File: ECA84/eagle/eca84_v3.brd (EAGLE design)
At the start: 222.9 x 127 mm, 186 parts

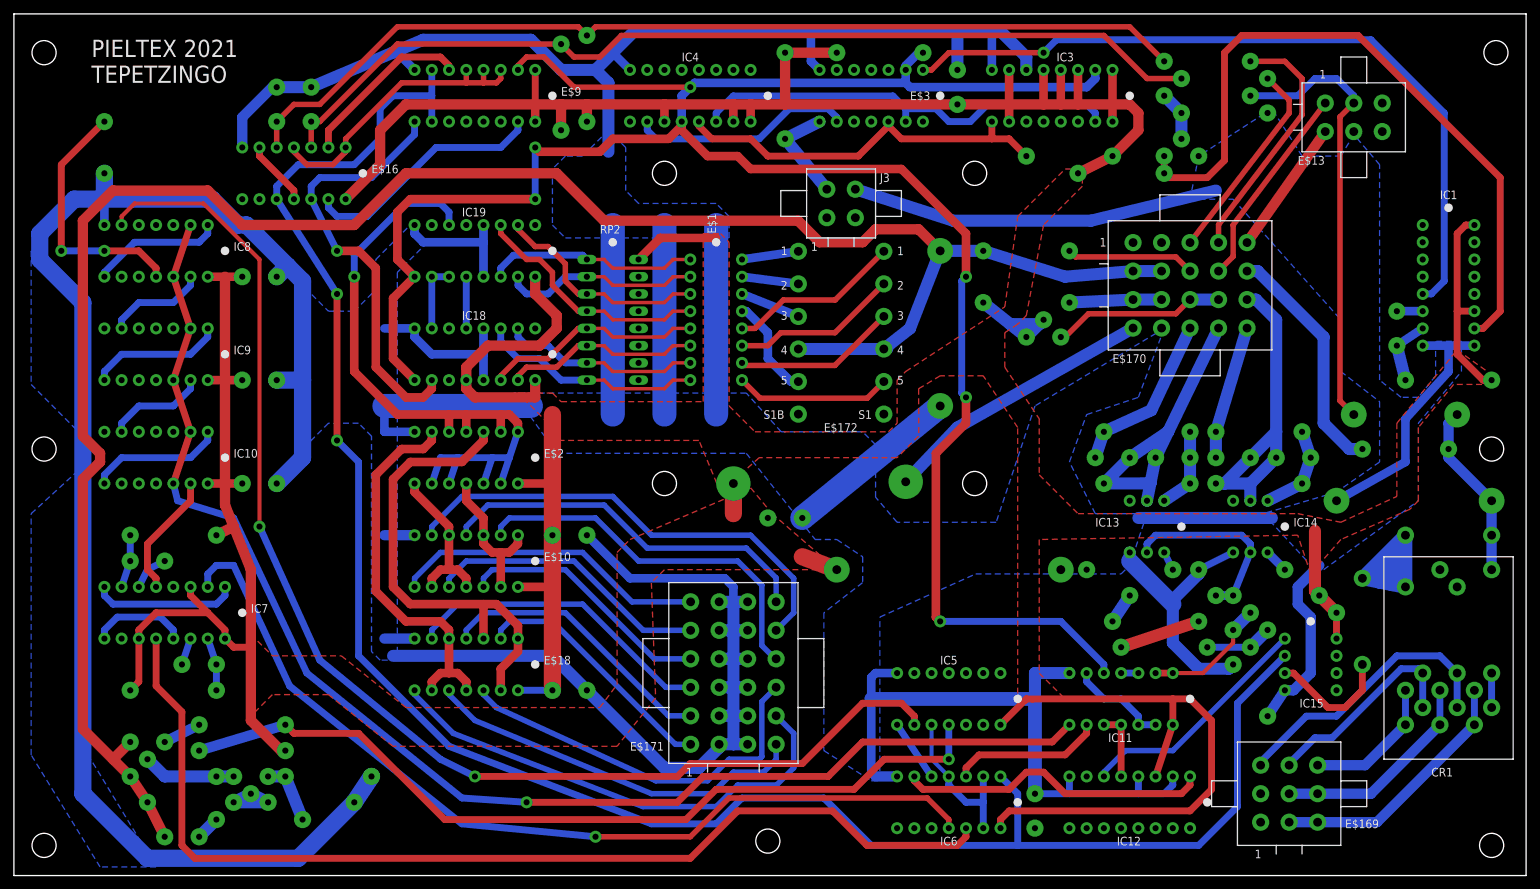
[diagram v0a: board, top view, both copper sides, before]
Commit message: ajustar orificios y exportar archivos CAM
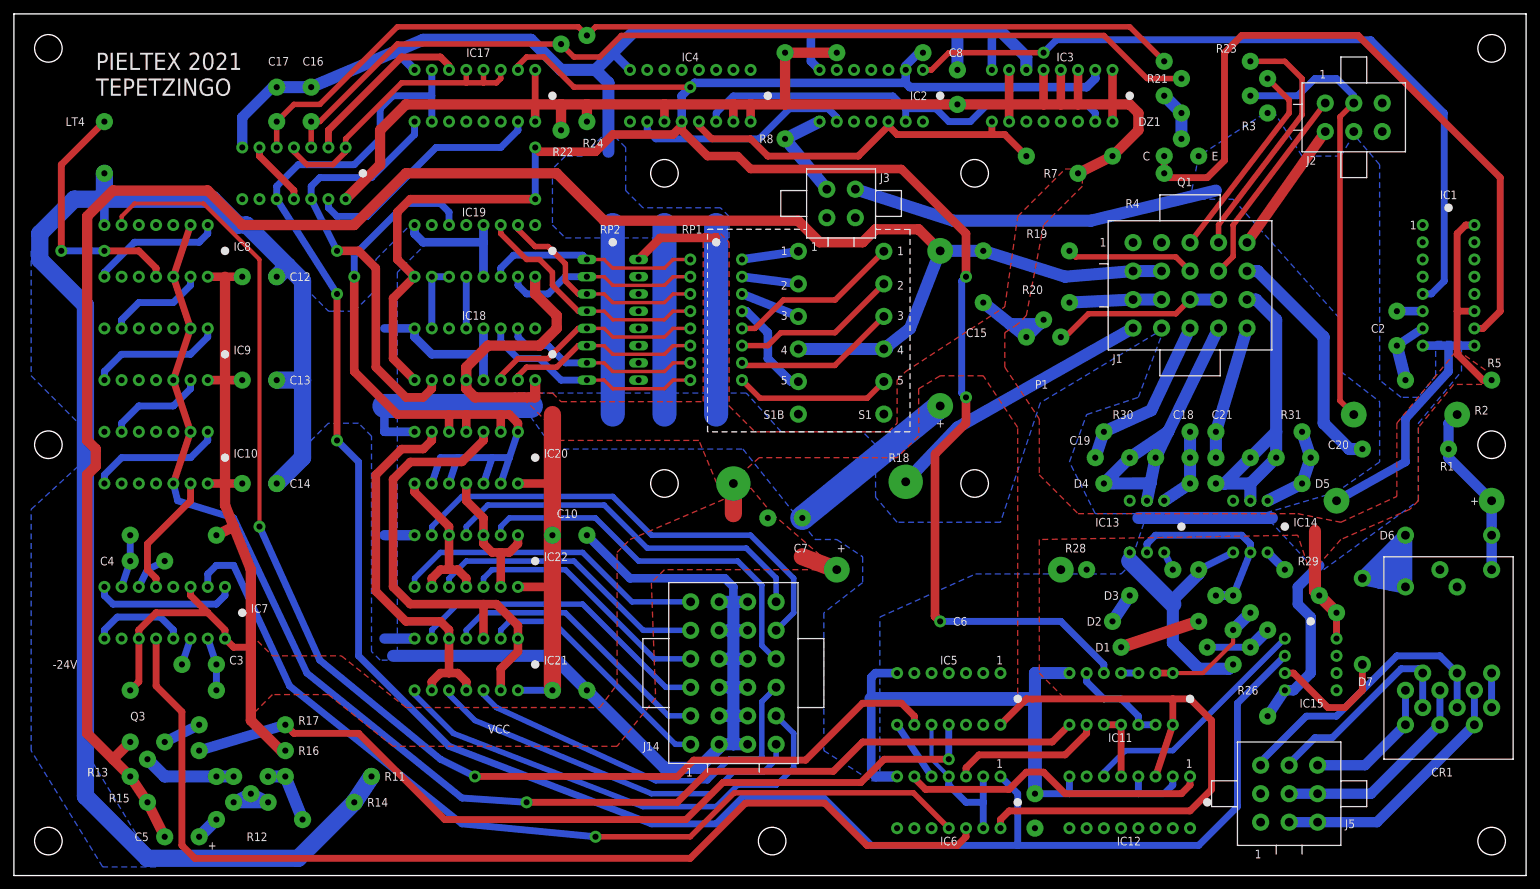
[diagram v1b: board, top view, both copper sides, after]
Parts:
- renumbered E$1 to RP1, E$10 to IC22, E$13 to J2, E$169 to J5, E$170 to J1, E$171 to J14, E$18 to IC21, E$2 to IC20, E$3 to IC2, E$9 to IC17
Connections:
- removed net S$45: IC11.P$14, IC12.P$3, IC5.P$14, IC6.P$14
- net VCC: now also IC11.P$14, IC12.P$3, IC5.P$14, IC6.P$14
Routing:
- net VCC: track 499.6 -> 589.9 mm
- net S$45: track 90.2 -> 0.00 mm
- net S$114: track 304.2 -> 302.6 mm
- net S$10: track 155.2 -> 156.2 mm
- net S$23: track 57.6 -> 57.0 mm
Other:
- board text added: "+"
- board text added: "-24V"
- board text added: "1"
- board text added: "C"
- board text added: "C10"
- board text added: "C12"
- board text added: "C13"
- board text added: "C14"
- board text added: "C15"
- board text added: "C16"
- board text added: "C17"
- board text added: "C18"
- board text added: "C19"
- board text added: "C2"
- board text added: "C20"
- board text added: "C21"
- board text added: "C3"
- board text added: "C4"
- board text added: "C5"
- board text added: "C6"
- board text added: "C7"
- board text added: "C8"
- board text added: "D1"
- board text added: "D2"
- board text added: "D3"
- board text added: "D4"
- board text added: "D5"
- board text added: "D6"
- board text added: "D7"
- board text added: "DZ1"
- board text added: "E"
- board text added: "LT4"
- board text added: "P1"
- board text added: "Q1"
- board text added: "Q3"
- board text added: "R1"
- board text added: "R11"
- board text added: "R12"
- board text added: "R13"
- board text added: "R14"
- board text added: "R15"
- board text added: "R16"
- board text added: "R17"
- board text added: "R18"
- board text added: "R19"
- board text added: "R2"
- board text added: "R20"
- board text added: "R21"
- board text added: "R22"
- board text added: "R23"
- board text added: "R24"
- board text added: "R26"
- board text added: "R28"
- board text added: "R29"
- board text added: "R3"
- board text added: "R30"
- board text added: "R31"
- board text added: "R4"
- board text added: "R5"
- board text added: "R7"
- board text added: "R8"
- board text added: "VCC"

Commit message: corrección pistas faltantes
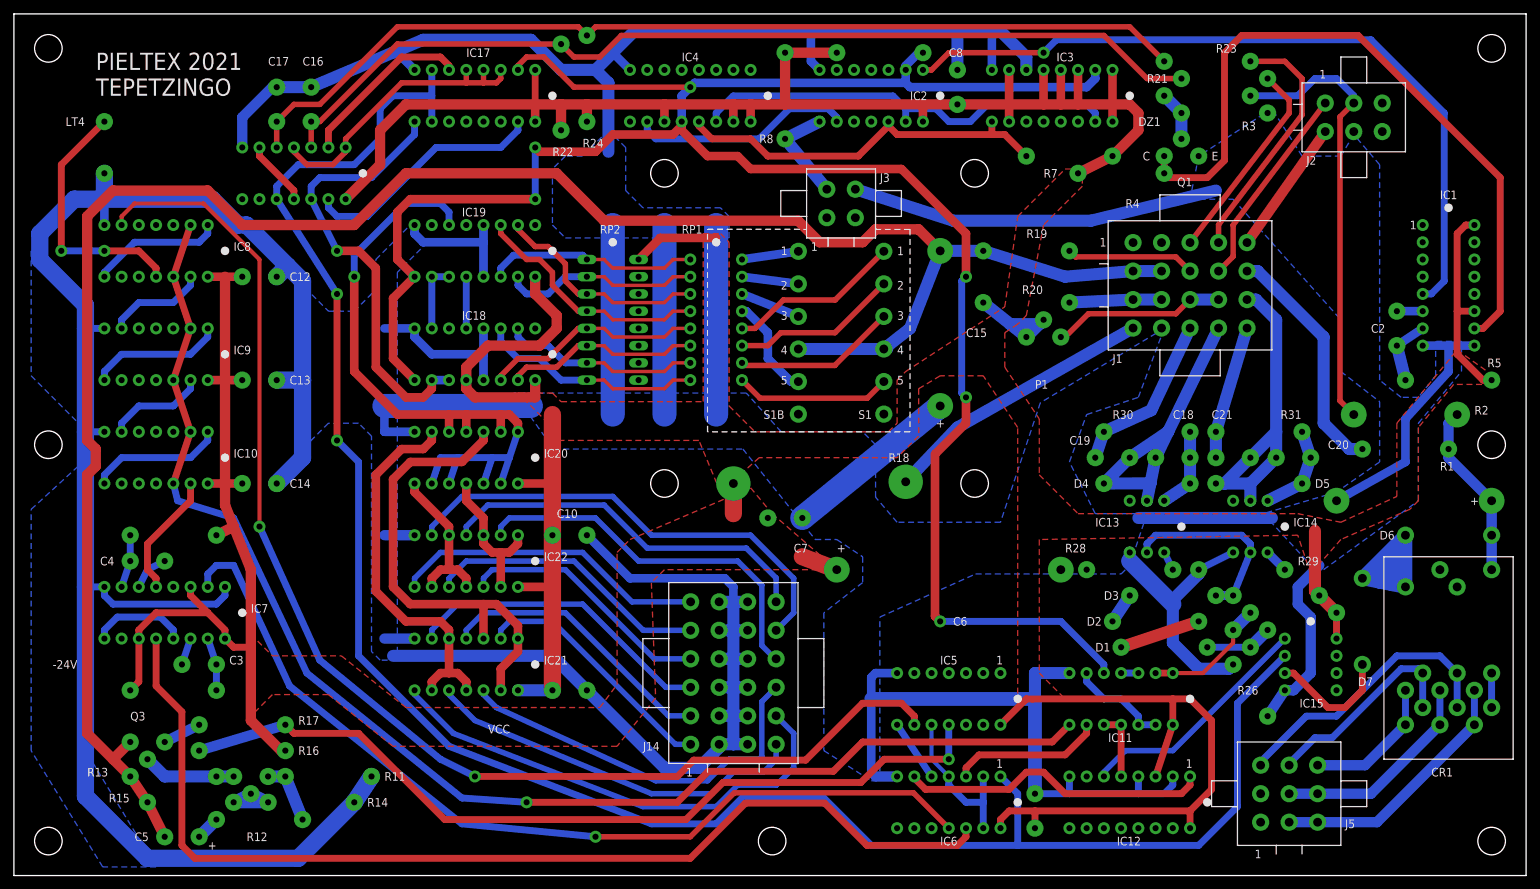
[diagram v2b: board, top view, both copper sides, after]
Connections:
- removed net S$57: IC7.P$1, IC7.P$8
- net GND: now also IC10.P$7, IC7.P$1, IC7.P$8, IC9.P$7
- net S$24: now also IC18.P$11
- net VCC: now also E$148.P$1, IC12.P$16, IC2.P$14
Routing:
- net GND: track 995.7 -> 1025.5 mm
- net S$57: track 21.4 -> 0.00 mm
- net VCC: track 589.9 -> 597.5 mm
- net S$24: track 64.0 -> 66.5 mm
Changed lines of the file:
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@@
 <wire x1="151.765" y1="118.745" x2="151.765" y2="113.665" width="1.27" layer="1"/>
 <contactref element="E$83" pad="P$1"/>
-<wire x1="113.665" y1="113.665" x2="139.065" y2="113.665" width="1.524" layer="1"/>
+<wire x1="113.665" y1="113.665" x2="133.985" y2="113.665" width="1.524" layer="1"/>
+<wire x1="133.985" y1="113.665" x2="139.065" y2="113.665" width="1.524" layer="1"/>
 <wire x1="139.065" y1="113.665" x2="146.685" y2="113.665" width="1.524" layer="1"/>
 <wire x1="146.685" y1="113.665" x2="151.765" y2="113.665" width="1.524" layer="1"/>
@@
 <wire x1="161.925" y1="106.045" x2="156.845" y2="103.505" width="1.524" layer="1"/>
 <contactref element="IC21" pad="P$14"/>
-<wire x1="74.295" y1="27.305" x2="79.375" y2="27.305" width="1.016" layer="16"/>
+<wire x1="74.295" y1="27.305" x2="79.375" y2="27.305" width="1.778" layer="16"/>
 <contactref element="E$14" pad="P$1"/>
 <wire x1="121.285" y1="45.085" x2="116.205" y2="46.99" width="2.54" layer="1"/>
@@
 <wire x1="145.415" y1="6.985" x2="145.415" y2="8.255" width="1.016" layer="1"/>
 <wire x1="145.415" y1="8.255" x2="146.685" y2="9.525" width="1.016" layer="1"/>
-<wire x1="146.685" y1="9.525" x2="173.355" y2="9.525" width="1.016" layer="1"/>
+<wire x1="146.685" y1="9.525" x2="150.495" y2="9.525" width="1.016" layer="1"/>
+<wire x1="150.495" y1="9.525" x2="173.355" y2="9.525" width="1.016" layer="1"/>
 <wire x1="173.355" y1="9.525" x2="176.53" y2="12.7" width="1.016" layer="1"/>
 <wire x1="176.53" y1="12.7" x2="176.53" y2="22.86" width="1.016" layer="1"/>
@@
 <contactref element="IC12" pad="P$3"/>
 <wire x1="168.275" y1="14.605" x2="170.815" y2="22.225" width="1.016" layer="1"/>
+<contactref element="E$148" pad="P$1"/>
+<contactref element="IC12" pad="P$16"/>
+<wire x1="150.495" y1="6.985" x2="150.495" y2="9.525" width="1.016" layer="1"/>
+<wire x1="173.355" y1="6.985" x2="173.355" y2="9.525" width="1.016" layer="1"/>
+<contactref element="IC2" pad="P$14"/>
+<wire x1="133.985" y1="111.125" x2="133.985" y2="113.665" width="1.27" layer="1"/>
 </signal>
 <signal name="S$10">
@@
 <wire x1="64.135" y1="97.79" x2="64.135" y2="95.885" width="1.016" layer="16"/>
 </signal>
-<signal name="S$24">
-<contactref element="E$58" pad="P$1"/>
-<wire x1="47.625" y1="92.075" x2="50.8" y2="92.075" width="1.27" layer="1"/>
-<wire x1="50.8" y1="92.075" x2="53.34" y2="89.535" width="1.27" layer="1"/>
-<wire x1="53.34" y1="89.535" x2="53.34" y2="74.93" width="1.27" layer="1"/>
-<wire x1="53.34" y1="74.93" x2="57.785" y2="70.485" width="1.27" layer="1"/>
-<wire x1="57.785" y1="70.485" x2="60.325" y2="70.485" width="1.27" layer="1"/>
-<contactref element="IC18" pad="P$10"/>
-<wire x1="60.325" y1="70.485" x2="61.595" y2="71.755" width="1.27" layer="1"/>
-<wire x1="61.595" y1="71.755" x2="61.595" y2="73.025" width="1.27" layer="1"/>
-<contactref element="E$16" pad="P$12"/>
-<contactref element="IC17" pad="P$9"/>
-<wire x1="43.815" y1="99.695" x2="43.815" y2="101.6" width="1.016" layer="16"/>
-<wire x1="43.815" y1="101.6" x2="45.085" y2="102.87" width="1.016" layer="16"/>
-<wire x1="45.085" y1="102.87" x2="52.705" y2="102.87" width="1.016" layer="16"/>
-<wire x1="52.705" y1="102.87" x2="59.055" y2="109.22" width="1.016" layer="16"/>
-<wire x1="59.055" y1="109.22" x2="59.055" y2="111.125" width="1.016" layer="16"/>
-<wire x1="47.625" y1="92.075" x2="43.815" y2="99.695" width="1.016" layer="16"/>
-</signal>
 <signal name="S$26">
 <contactref element="IC19" pad="P$2"/>
@@
 <wire x1="23.495" y1="36.195" x2="23.495" y2="34.925" width="1.016" layer="16"/>
 </signal>
-<signal name="S$57">
-<contactref element="IC7" pad="P$1"/>
-<contactref element="IC7" pad="P$8"/>
-<wire x1="13.335" y1="42.545" x2="13.335" y2="41.275" width="1.016" layer="16"/>
-<wire x1="13.335" y1="41.275" x2="14.605" y2="40.005" width="1.016" layer="16"/>
-<wire x1="14.605" y1="40.005" x2="29.845" y2="40.005" width="1.016" layer="16"/>
-<wire x1="29.845" y1="40.005" x2="31.115" y2="41.275" width="1.016" layer="16"/>
-<wire x1="31.115" y1="41.275" x2="31.115" y2="42.545" width="1.016" layer="16"/>
-</signal>
 <signal name="S$58">
 <contactref element="E$30" pad="P$1"/>
@@
 <wire x1="8.89" y1="99.695" x2="3.81" y2="94.615" width="2.54" layer="16"/>
 <wire x1="3.81" y1="90.805" x2="10.541" y2="84.074" width="2.54" layer="16"/>
-<wire x1="10.541" y1="84.074" x2="10.541" y2="11.684" width="2.54" layer="16"/>
+<wire x1="10.541" y1="84.074" x2="10.541" y2="80.645" width="2.54" layer="16"/>
+<wire x1="10.541" y1="80.645" x2="10.541" y2="65.405" width="2.54" layer="16"/>
+<wire x1="10.541" y1="65.405" x2="10.541" y2="42.545" width="2.54" layer="16"/>
+<wire x1="10.541" y1="42.545" x2="10.541" y2="11.684" width="2.54" layer="16"/>
 <wire x1="10.541" y1="11.684" x2="19.685" y2="2.54" width="2.54" layer="16"/>
 <wire x1="19.685" y1="2.54" x2="41.91" y2="2.54" width="2.54" layer="16"/>
@@
 <wire x1="127" y1="14.605" x2="126.365" y2="15.24" width="1.27" layer="16"/>
 <wire x1="126.365" y1="15.24" x2="126.365" y2="26.035" width="1.27" layer="16"/>
+<contactref element="IC9" pad="P$7"/>
+<contactref element="IC10" pad="P$7"/>
+<contactref element="IC7" pad="P$1"/>
+<contactref element="IC7" pad="P$8"/>
+<wire x1="13.335" y1="42.545" x2="13.335" y2="41.275" width="1.016" layer="16"/>
+<wire x1="13.335" y1="41.275" x2="14.605" y2="40.005" width="1.016" layer="16"/>
+<wire x1="14.605" y1="40.005" x2="29.845" y2="40.005" width="1.016" layer="16"/>
+<wire x1="29.845" y1="40.005" x2="31.115" y2="41.275" width="1.016" layer="16"/>
+<wire x1="31.115" y1="41.275" x2="31.115" y2="42.545" width="1.016" layer="16"/>
+<wire x1="13.335" y1="80.645" x2="10.541" y2="80.645" width="1.016" layer="16"/>
+<wire x1="13.335" y1="65.405" x2="10.541" y2="65.405" width="1.016" layer="16"/>
+<wire x1="13.335" y1="42.545" x2="10.541" y2="42.545" width="1.016" layer="16"/>
+</signal>
+<signal name="S$24">
+<contactref element="IC17" pad="P$9"/>
+<wire x1="59.055" y1="109.22" x2="59.055" y2="111.125" width="1.016" layer="16"/>
+<wire x1="52.705" y1="102.87" x2="59.055" y2="109.22" width="1.016" layer="16"/>
+<wire x1="45.085" y1="102.87" x2="52.705" y2="102.87" width="1.016" layer="16"/>
+<wire x1="43.815" y1="101.6" x2="45.085" y2="102.87" width="1.016" layer="16"/>
+<contactref element="E$16" pad="P$12"/>
+<wire x1="43.815" y1="99.695" x2="43.815" y2="101.6" width="1.016" layer="16"/>
+<wire x1="47.625" y1="92.075" x2="43.815" y2="99.695" width="1.016" layer="16"/>
+<contactref element="E$58" pad="P$1"/>
+<contactref element="IC18" pad="P$10"/>
+<wire x1="47.625" y1="92.075" x2="50.8" y2="92.075" width="1.27" layer="1"/>
+<wire x1="50.8" y1="92.075" x2="53.34" y2="89.535" width="1.27" layer="1"/>
+<wire x1="61.595" y1="71.755" x2="61.595" y2="73.025" width="1.27" layer="1"/>
+<wire x1="60.325" y1="70.485" x2="61.595" y2="71.755" width="1.27" layer="1"/>
+<wire x1="53.34" y1="89.535" x2="53.34" y2="74.93" width="1.27" layer="1"/>
+<wire x1="53.34" y1="74.93" x2="57.785" y2="70.485" width="1.27" layer="1"/>
+<wire x1="57.785" y1="70.485" x2="60.325" y2="70.485" width="1.27" layer="1"/>
+<contactref element="IC18" pad="P$11"/>
+<wire x1="61.595" y1="73.025" x2="64.135" y2="73.025" width="1.27" layer="16"/>
 </signal>
 <signal name="S$65">
